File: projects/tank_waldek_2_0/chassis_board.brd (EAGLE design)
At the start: 73 x 80 mm, 19 parts, among them U1 NUCLEO-L432KC

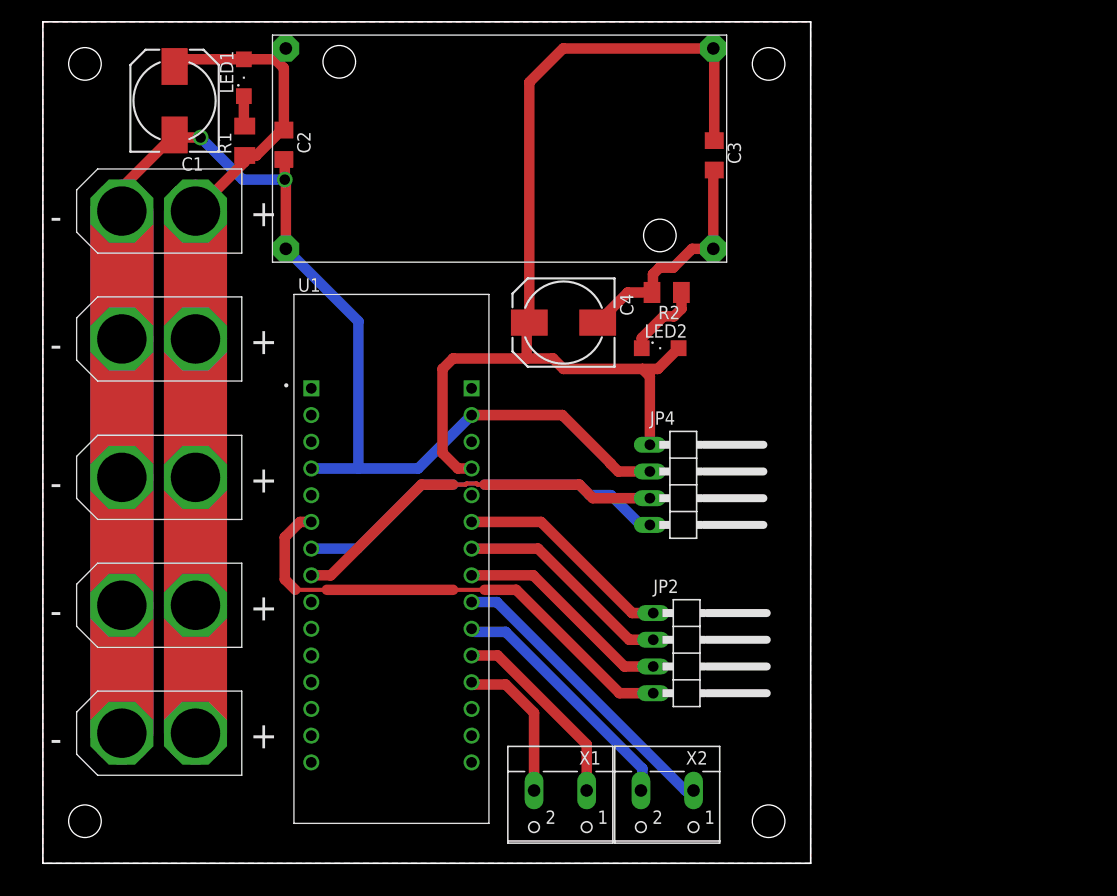
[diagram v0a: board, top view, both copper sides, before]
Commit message: miniaturized chassis board
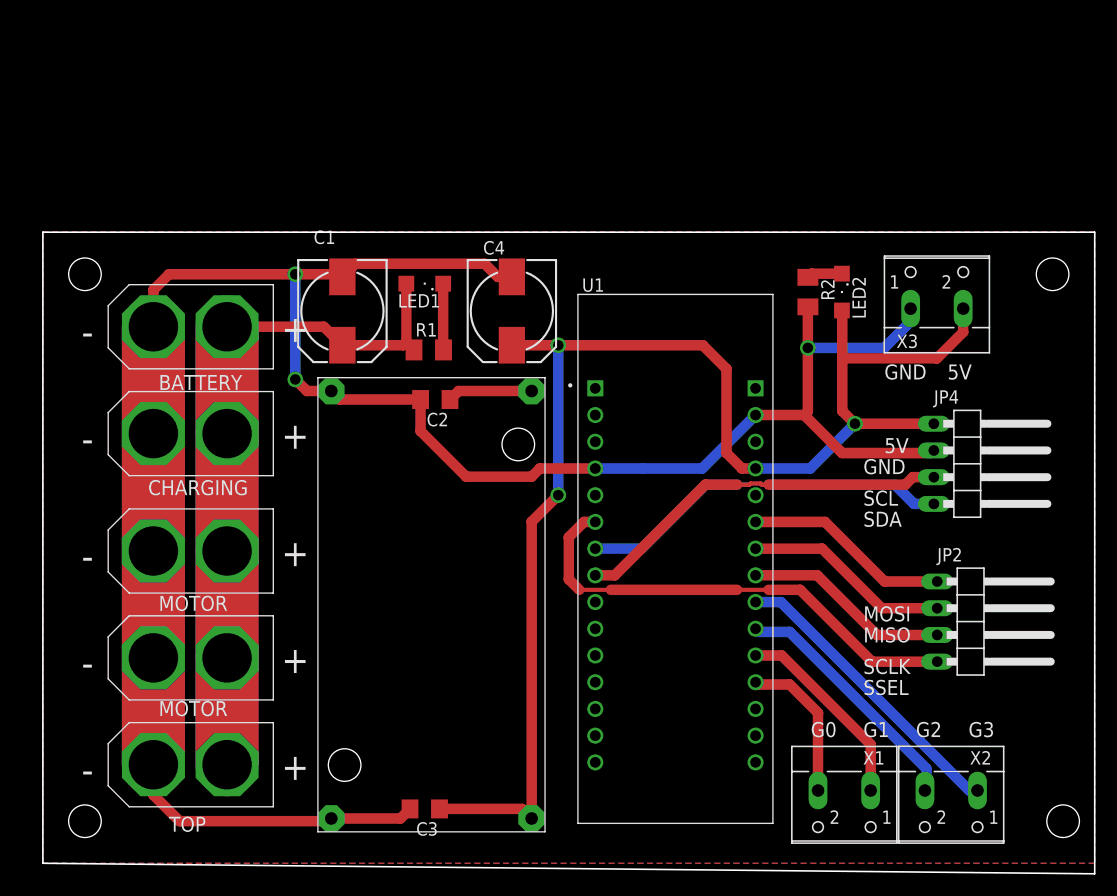
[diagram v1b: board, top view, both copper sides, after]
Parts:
- added X3: (no value), con-wago-500:W237-102
- moved C3 68.0 mm to (36.3, 5.17), turned to 180 degrees
- moved U$6 66.7 mm to (26.1, 2.99), turned to 0 degrees
- moved C2 28.2 mm to (37.3, 44.1), turned to 180 degrees
- moved JP2 27.2 mm to (88.8, 23.0)
- moved JP4 27.1 mm to (88.5, 38.0)
- moved U1 27.0 mm to (60.1, 28.9)
- moved X1 27.0 mm to (76.2, 5.65)
- moved X2 27.0 mm to (86.4, 5.65)
- moved R1 26.5 mm to (36.7, 48.8), turned to 0 degrees
- moved LED1 26.1 mm to (36.3, 55.1), turned to 180 degrees
- moved C1 25.6 mm to (28.5, 52.5), turned to 270 degrees
- moved LED2 18.1 mm to (76.0, 54.3), turned to 270 degrees
- moved R2 13.4 mm to (72.7, 54.3), turned to 270 degrees
- moved U$5 11.4 mm to (21.9, 55.0)
- moved U$4 9.49 mm to (21.9, 44.9)
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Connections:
- removed net N$3: C3.2, C4.-, R2.2, U$6.GND_OUT
- net GND: now also C3.2, C4.-, R2.2, U$6.GND_OUT, X3.1
- net VCC: now also X3.2
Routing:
- net GND: track 189.7 -> 254.5 mm, vias 2 -> 3
- net VCC: track 97.9 -> 132.6 mm, vias 0 -> 3
- net N$3: track 22.4 -> 0.00 mm
- net N$1: track 130.3 -> 116.6 mm
- net N$2: track 7.45 -> 3.38 mm
- net N$4: track 2.88 -> 6.31 mm
- net SCLK: track 20.9 -> 19.6 mm
- net MOSI: track 20.9 -> 19.6 mm
- net MISO: track 20.9 -> 19.6 mm
- net SSEL: track 46.6 -> 45.4 mm
- net SDA: track 36.4 -> 35.6 mm
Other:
- board size 73 x 80 mm -> 100 x 61 mm
